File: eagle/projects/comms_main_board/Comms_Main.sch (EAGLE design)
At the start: 12 parts, among them U1 TPS562209DDCT, U2 LP2985-33DBVR

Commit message: Worked on comms power management portion of schematic more
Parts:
- added C10: 100nF, comms:CAP_100NF0_0805
- added C11: 22uF, comms:CAP_22UF0_1210
- added C12: 22uF, comms:CAP_22UF0_1206
- added C13: 4.7uF, comms:CAP_4UH7_0805
- added C8, C9: 1uF, comms:CAP_1UF0_0603
- added L2: 4.7uH, comms:L_4UH7
- added R3: 56.2k, comms:RES_56R2_0603
- added R4: 10k, comms:RES_10R0_0603
- added R5: 174k, comms:RES_174R0_0603
- added R6: 25.5k, comms:RES_25R5_0603
- added U3: LP5900TLX-3.3/NOPB, comms:LP5900TLX-3.3/NOPB
- added U4: TPS562209DDCT, comms:TPS562209DDCR
- added U5: LMZ34002RKGR, comms:LMZ34002RKGR
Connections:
- new net 11P1V_IN: C11.1, U4.EN, U4.VIN
- new net 12V_BOARD: R5.2
- new net 3P3V_ATV: C9.1, U3.VOUT
- new net 5V_BOARD: C12.1, C8.1, L2.2, R3.2, U3.VEN, U3.VIN
- new net N$5: C10.1, U4.VBST
- new net N$6: C10.2, L2.1, U4.SW
- new net N$7: R3.1, R4.2, U4.VFB
- new net N$8: C11.2, C12.2, R4.1, U4.GND
- new net N$9: R6.2
- net GND: now also C8.2, C9.2, U3.GND
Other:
- note added: "COMMS 11.1V Battery Power Management"

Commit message: Working on parts for comms power management more
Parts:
- added C14: 100uF, comms:CAP_100UF0_1206
- added R7: 53.6k, comms:RES_53R6_0603
- added U6: LM3488MMX/NOPB, comms:LM3488MMX/NOPB
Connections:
- new net N$10: R7.2
- new net NEG_5V_BOARD: U5.A_VOUT_2, U5.A_VOUT_3, U5.A_VOUT_5, U5.RT
- net GND: now also U5.GND_2, U5.GND_5
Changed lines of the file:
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@@
 <part name="R6" library="comms" deviceset="RES" device="_0603" technology="_25R5" value="25.5k"/>
 <part name="C13" library="comms" deviceset="CAP" device="_0805" technology="_4UH7" value="4.7uF"/>
+<part name="R7" library="comms" deviceset="RES" device="_0603" technology="_53R6" value="53.6k"/>
+<part name="SUPPLY4" library="supply2" deviceset="GND" device=""/>
+<part name="C14" library="comms" deviceset="CAP" device="_1206" technology="_100UF0" value="100uF"/>
+<part name="FRAME3" library="frames" deviceset="A4L-LOC" device=""/>
+<part name="U6" library="comms" deviceset="LM3488" device="" technology="MMX/NOPB" value="LM3488MMX/NOPB"/>
 </parts>
 <sheets>
@@
 <sheet>
 <plain>
+<text x="-67.056" y="73.66" size="5.08" layer="91">COMMS 11.1V Battery Power Management</text>
+</plain>
+<instances>
+<instance part="FRAME3" gate="G$1" x="-129.54" y="-93.98"/>
+<instance part="U6" gate="A" x="-33.02" y="2.54"/>
+</instances>
+<busses>
+</busses>
+<nets>
+</nets>
+</sheet>
+<sheet>
+<plain>
 <text x="108.966" y="115.316" size="5.08" layer="91">COMMS 11.1V Battery Power Management</text>
 </plain>
@@
 <instance part="R6" gate="G$1" x="68.58" y="27.94" rot="R90"/>
 <instance part="C13" gate="G$1" x="58.42" y="38.1"/>
+<instance part="R7" gate="G$1" x="149.86" y="-15.24" rot="R90"/>
+<instance part="SUPPLY4" gate="GND" x="119.38" y="-45.72"/>
+<instance part="C14" gate="G$1" x="170.18" y="27.94"/>
 </instances>
 <busses>
@@
 <pinref part="C8" gate="G$1" pin="2"/>
 <pinref part="C9" gate="G$1" pin="2"/>
+</segment>
+<segment>
+<wire x1="58.42" y1="35.814" x2="58.42" y2="-43.18" width="0.1524" layer="91"/>
+<wire x1="58.42" y1="-43.18" x2="119.38" y2="-43.18" width="0.1524" layer="91"/>
+<pinref part="SUPPLY4" gate="GND" pin="GND"/>
+<wire x1="119.38" y1="-43.18" x2="144.78" y2="-43.18" width="0.1524" layer="91"/>
+<junction x="119.38" y="-43.18"/>
+<wire x1="139.446" y1="-12.7" x2="144.78" y2="-12.7" width="0.1524" layer="91"/>
+<wire x1="144.78" y1="-12.7" x2="144.78" y2="-15.24" width="0.1524" layer="91"/>
+<junction x="144.78" y="-43.18"/>
+<pinref part="U5" gate="A" pin="GND_5"/>
+<wire x1="144.78" y1="-15.24" x2="144.78" y2="-17.78" width="0.1524" layer="91"/>
+<wire x1="144.78" y1="-17.78" x2="144.78" y2="-20.32" width="0.1524" layer="91"/>
+<wire x1="144.78" y1="-20.32" x2="144.78" y2="-22.86" width="0.1524" layer="91"/>
+<wire x1="144.78" y1="-22.86" x2="144.78" y2="-25.4" width="0.1524" layer="91"/>
+<wire x1="144.78" y1="-25.4" x2="144.78" y2="-27.94" width="0.1524" layer="91"/>
+<wire x1="144.78" y1="-27.94" x2="144.78" y2="-43.18" width="0.1524" layer="91"/>
+<wire x1="139.7" y1="-15.24" x2="144.78" y2="-15.24" width="0.1524" layer="91"/>
+<junction x="144.78" y="-15.24"/>
+<wire x1="139.446" y1="-17.78" x2="144.78" y2="-17.78" width="0.1524" layer="91"/>
+<junction x="144.78" y="-17.78"/>
+<wire x1="139.446" y1="-20.32" x2="144.78" y2="-20.32" width="0.1524" layer="91"/>
+<junction x="144.78" y="-20.32"/>
+<pinref part="U5" gate="A" pin="GND_2"/>
+<wire x1="139.7" y1="-22.86" x2="144.78" y2="-22.86" width="0.1524" layer="91"/>
+<junction x="144.78" y="-22.86"/>
+<wire x1="139.446" y1="-25.4" x2="144.78" y2="-25.4" width="0.1524" layer="91"/>
+<junction x="144.78" y="-25.4"/>
+<wire x1="139.446" y1="-27.94" x2="144.78" y2="-27.94" width="0.1524" layer="91"/>
+<junction x="144.78" y="-27.94"/>
+<wire x1="170.18" y1="25.654" x2="170.18" y2="-43.18" width="0.1524" layer="91"/>
+<wire x1="170.18" y1="-43.18" x2="149.86" y2="-43.18" width="0.1524" layer="91"/>
+<wire x1="149.86" y1="-43.18" x2="144.78" y2="-43.18" width="0.1524" layer="91"/>
+<wire x1="149.86" y1="-20.066" x2="149.86" y2="-43.18" width="0.1524" layer="91"/>
+<junction x="149.86" y="-43.18"/>
 </segment>
 </net>
@@
 <segment>
 <wire x1="101.854" y1="48.26" x2="68.58" y2="48.26" width="0.1524" layer="91"/>
-<label x="55.88" y="48.26" size="5.08" layer="95"/>
+<label x="55.88" y="48.26" size="1.778" layer="95"/>
 <pinref part="R5" gate="G$1" pin="2"/>
 <wire x1="68.58" y1="48.26" x2="58.42" y2="48.26" width="0.1524" layer="91"/>
@@
 </segment>
 </net>
+<net name="NEG_5V_BOARD" class="0">
+<segment>
+<wire x1="139.192" y1="48.26" x2="144.018" y2="48.26" width="0.1524" layer="91"/>
+<label x="172.72" y="48.26" size="1.778" layer="95"/>
+<wire x1="144.018" y1="48.26" x2="157.48" y2="48.26" width="0.1524" layer="91"/>
+<wire x1="157.48" y1="48.26" x2="170.18" y2="48.26" width="0.1524" layer="91"/>
+<wire x1="170.18" y1="48.26" x2="182.88" y2="48.26" width="0.1524" layer="91"/>
+<wire x1="139.446" y1="45.72" x2="144.018" y2="45.72" width="0.1524" layer="91"/>
+<wire x1="144.018" y1="45.72" x2="144.018" y2="48.26" width="0.1524" layer="91"/>
+<junction x="144.018" y="48.26"/>
+<wire x1="139.446" y1="43.18" x2="144.018" y2="43.18" width="0.1524" layer="91"/>
+<wire x1="144.018" y1="43.18" x2="144.018" y2="45.72" width="0.1524" layer="91"/>
+<junction x="144.018" y="45.72"/>
+<wire x1="139.192" y1="40.64" x2="144.018" y2="40.64" width="0.1524" layer="91"/>
+<wire x1="144.018" y1="40.64" x2="144.018" y2="43.18" width="0.1524" layer="91"/>
+<junction x="144.018" y="43.18"/>
+<wire x1="139.192" y1="38.1" x2="144.018" y2="38.1" width="0.1524" layer="91"/>
+<wire x1="144.018" y1="38.1" x2="144.018" y2="40.64" width="0.1524" layer="91"/>
+<junction x="144.018" y="40.64"/>
+<wire x1="139.446" y1="35.56" x2="144.018" y2="35.56" width="0.1524" layer="91"/>
+<wire x1="144.018" y1="35.56" x2="144.018" y2="38.1" width="0.1524" layer="91"/>
+<junction x="144.018" y="38.1"/>
+<wire x1="170.18" y1="32.766" x2="170.18" y2="48.26" width="0.1524" layer="91"/>
+<junction x="170.18" y="48.26"/>
+<pinref part="U5" gate="A" pin="RT"/>
+<wire x1="139.7" y1="30.48" x2="157.48" y2="30.48" width="0.1524" layer="91"/>
+<wire x1="157.48" y1="30.48" x2="157.48" y2="48.26" width="0.1524" layer="91"/>
+<junction x="157.48" y="48.26"/>
+<wire x1="157.48" y1="30.48" x2="157.48" y2="22.86" width="0.1524" layer="91"/>
+<junction x="157.48" y="30.48"/>
+<wire x1="157.48" y1="22.86" x2="157.48" y2="20.32" width="0.1524" layer="91"/>
+<wire x1="157.48" y1="20.32" x2="157.48" y2="11.684" width="0.1524" layer="91"/>
+<wire x1="139.446" y1="12.7" x2="147.32" y2="12.7" width="0.1524" layer="91"/>
+<pinref part="U5" gate="A" pin="A_VOUT_3"/>
+<wire x1="147.32" y1="12.7" x2="147.32" y2="11.684" width="0.1524" layer="91"/>
+<wire x1="147.32" y1="11.684" x2="147.32" y2="10.16" width="0.1524" layer="91"/>
+<wire x1="147.32" y1="10.16" x2="147.32" y2="7.62" width="0.1524" layer="91"/>
+<wire x1="147.32" y1="7.62" x2="147.32" y2="5.08" width="0.1524" layer="91"/>
+<wire x1="147.32" y1="5.08" x2="147.32" y2="2.54" width="0.1524" layer="91"/>
+<wire x1="147.32" y1="2.54" x2="147.32" y2="0" width="0.1524" layer="91"/>
+<wire x1="147.32" y1="0" x2="147.32" y2="-2.54" width="0.1524" layer="91"/>
+<wire x1="147.32" y1="-2.54" x2="139.7" y2="-2.54" width="0.1524" layer="91"/>
+<wire x1="139.446" y1="0" x2="147.32" y2="0" width="0.1524" layer="91"/>
+<junction x="147.32" y="0"/>
+<pinref part="U5" gate="A" pin="A_VOUT_5"/>
+<wire x1="139.7" y1="2.54" x2="147.32" y2="2.54" width="0.1524" layer="91"/>
+<junction x="147.32" y="2.54"/>
+<pinref part="U5" gate="A" pin="A_VOUT_2"/>
+<wire x1="139.7" y1="5.08" x2="147.32" y2="5.08" width="0.1524" layer="91"/>
+<junction x="147.32" y="5.08"/>
+<wire x1="139.446" y1="7.62" x2="147.32" y2="7.62" width="0.1524" layer="91"/>
+<junction x="147.32" y="7.62"/>
+<wire x1="139.446" y1="10.16" x2="147.32" y2="10.16" width="0.1524" layer="91"/>
+<junction x="147.32" y="10.16"/>
+<wire x1="147.32" y1="11.684" x2="157.48" y2="11.684" width="0.1524" layer="91"/>
+<junction x="147.32" y="11.684"/>
+<wire x1="157.48" y1="11.684" x2="157.48" y2="-38.1" width="0.1524" layer="91"/>
+<junction x="157.48" y="11.684"/>
+<wire x1="157.48" y1="-38.1" x2="76.2" y2="-38.1" width="0.1524" layer="91"/>
+<wire x1="76.2" y1="-38.1" x2="68.58" y2="-38.1" width="0.1524" layer="91"/>
+<wire x1="68.58" y1="-38.1" x2="68.58" y2="23.622" width="0.1524" layer="91"/>
+<wire x1="102.616" y1="33.02" x2="76.2" y2="33.02" width="0.1524" layer="91"/>
+<wire x1="76.2" y1="33.02" x2="76.2" y2="-38.1" width="0.1524" layer="91"/>
+<junction x="76.2" y="-38.1"/>
+<wire x1="139.446" y1="22.86" x2="157.48" y2="22.86" width="0.1524" layer="91"/>
+<junction x="157.48" y="22.86"/>
+<wire x1="139.446" y1="20.32" x2="157.48" y2="20.32" width="0.1524" layer="91"/>
+<junction x="157.48" y="20.32"/>
+</segment>
+</net>
+<net name="N$10" class="0">
+<segment>
+<wire x1="139.446" y1="-7.62" x2="149.86" y2="-7.62" width="0.1524" layer="91"/>
+<pinref part="R7" gate="G$1" pin="2"/>
+<wire x1="149.86" y1="-10.16" x2="149.86" y2="-7.62" width="0.1524" layer="91"/>
+</segment>
+</net>

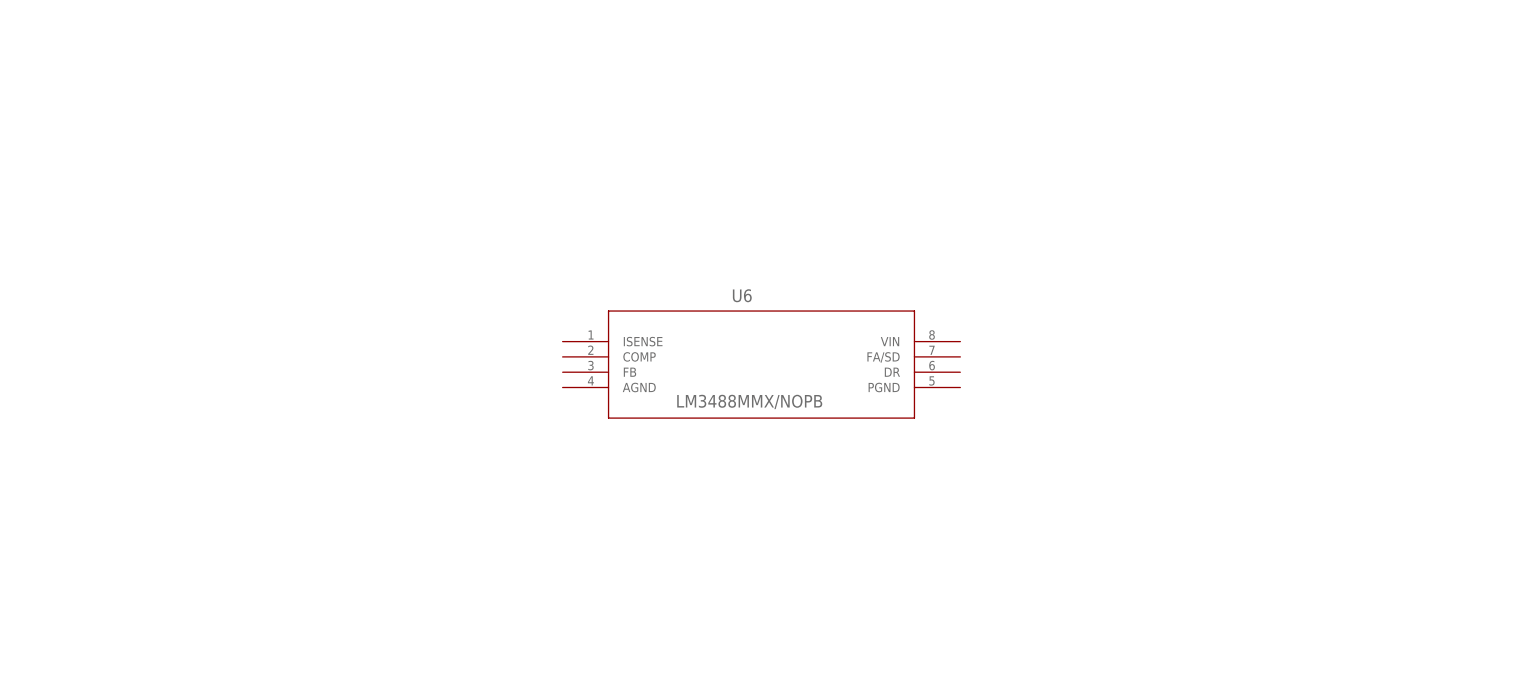
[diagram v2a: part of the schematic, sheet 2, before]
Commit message: Finished comms power management schematic
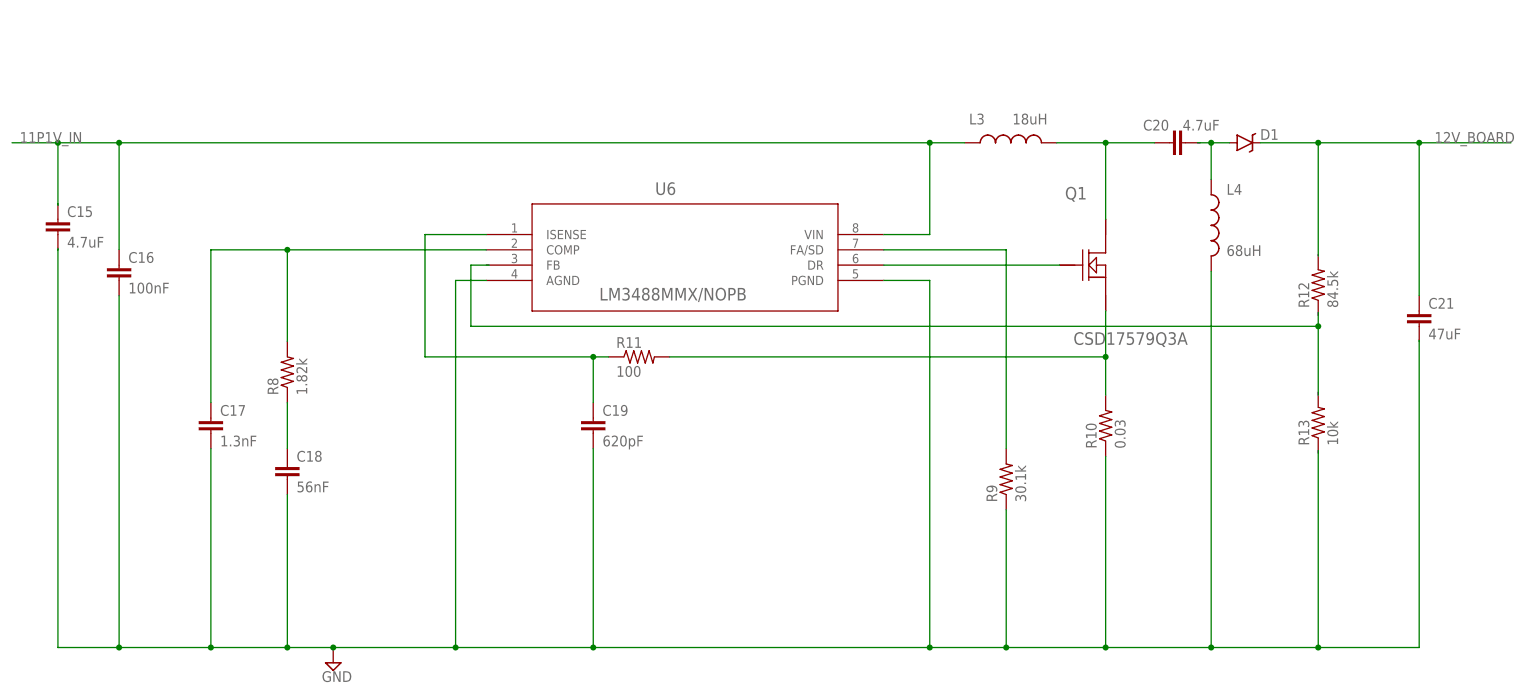
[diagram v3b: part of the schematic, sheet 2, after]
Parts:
- added C15: 4.7uF, comms:CAP_4UH7_1210
- added C16: 100nF, comms:CAP_100NF0_0805
- added C17: 1.3nF, comms:CAP_1NF3_0805
- added C18: 56nF, comms:CAP_56NF0_0603
- added C19: 620pF, comms:CAP_620PF0_0805
- added C20: 4.7uF, comms:CAP_4UH7_0805
- added C21: 47uF, comms:CAP_47UF0_1210
- added D1: (no value), comms:DIODE-SCHOTTKY_DO-214AC
- added L3: 18uH, comms:L_18UH0-180ML
- added L4: 68uH, comms:L_68UH0-680ML
- added Q1: CSD17579Q3A, comms:CSD17579Q3A
- added R10: 0.03, comms:RES_0RS030_0805
- added R11: 100, comms:RES_0R100_0603
- added R12: 84.5k, comms:RES_84R5_0603
- added R13: 10k, comms:RES_10R0_0603
- added R8: 1.82k, comms:RES_1R82_0805
- added R9: 30.1k, comms:RES_30R1_0603
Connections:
- new net N$11: U5.PH, U5.PH_2, U5.PH_3, U5.PH_4, U5.PH_5
- new net N$12: C18.1, R8.1
- new net N$13: C17.1, R8.2, U6.COMP
- new net N$14: R9.2, U6.FA/SD
- new net N$15: C19.1, R11.1, U6.ISENSE
- new net N$16: Q1.GATE, U6.DR
- new net N$17: Q1.SOURCE_2, R10.2, R11.2
- new net N$18: C20.1, L3.2, Q1.DRAIN_2
- new net N$19: D1.A, L4.1
- net 11P1V_IN: now also C15.1, C16.1, L3.1, U6.VIN
- net 12V_BOARD: now also C21.1, D1.C
- net GND: now also C15.2, C16.2, C17.2, C18.2, C19.2, L4.2, R10.1, R9.1, U6.AGND, U6.PGND
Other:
- moved on the sheet: U6

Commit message: Max-m8q gps sch
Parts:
- added C22: 10nF, comms:CAP_10NF0_0805
- added J1: RECE-20279-001E, comms:IPEX-20279-001E
- added L5: 27nH, comms:L_27NH0_0603
- added R14, R15: 4.7k, daqcs:RES_4R7_0603
- added R16: 10, comms:RES_0R10_0603
- added U$1: MAX-M8Q, comms:UBLOX_MAX
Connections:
- new net 3P3V_ACC: R14.2, R15.2
- new net GPS_SCL: R15.1, U$1.17_SCL2
- new net GPS_SDA: R14.1, U$1.16_SDA2
- new net N$20: R16.2, U$1.15_RESERVED
- new net N$22: C22.1, R16.1
- new net N$24: J1.1, L5.1, U$1.11_RF_IN
- net 3P3V_SENSORS: now also U$1.6_V_BCKP, U$1.7_VCC_IO, U$1.8_VCC
- net GND: now also C22.2, J1.GND@1, U$1.10_GND, U$1.12_GND, U$1.1_GND
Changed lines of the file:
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@@
 <part name="C21" library="comms" deviceset="CAP" device="_1210" technology="_47UF0" value="47uF"/>
 <part name="L4" library="comms" deviceset="L" device="-680ML" technology="_68UH0" value="68uH"/>
+<part name="FRAME4" library="frames" deviceset="A4L-LOC" device=""/>
+<part name="U$1" library="comms" deviceset="UBLOX_MAX" device="" value="MAX-M8Q"/>
+<part name="R14" library="daqcs" deviceset="RES" device="_0603" technology="_4R7" value="4.7k"/>
+<part name="R15" library="daqcs" deviceset="RES" device="_0603" technology="_4R7" value="4.7k"/>
+<part name="SUPPLY6" library="supply2" deviceset="GND" device=""/>
+<part name="J1" library="comms" deviceset="IPEX-20279-001E" device="" value="RECE-20279-001E"/>
+<part name="R16" library="comms" deviceset="RES" device="_0603" technology="_0R10" value="10"/>
+<part name="C22" library="comms" deviceset="CAP" device="_0805" technology="_10NF0" value="10nF"/>
+<part name="L5" library="comms" deviceset="L" device="_0603" technology="_27NH0" value="27nH"/>
 </parts>
 <sheets>
@@
 </segment>
 </net>
+</nets>
+</sheet>
+<sheet>
+<plain>
+</plain>
+<instances>
+<instance part="FRAME4" gate="G$1" x="0" y="0"/>
+<instance part="U$1" gate="G$1" x="134.62" y="106.68"/>
+<instance part="R14" gate="G$1" x="50.8" y="101.6" rot="R90"/>
+<instance part="R15" gate="G$1" x="38.1" y="101.6" rot="R90"/>
+<instance part="SUPPLY6" gate="GND" x="99.06" y="68.58"/>
+<instance part="J1" gate="G$1" x="55.88" y="116.84"/>
+<instance part="R16" gate="G$1" x="91.44" y="96.52"/>
+<instance part="C22" gate="G$1" x="76.2" y="78.74"/>
+<instance part="L5" gate="G$1" x="76.2" y="104.14"/>
+</instances>
+<busses>
+</busses>
+<nets>
+<net name="3P3V_SENSORS" class="0">
+<segment>
+<pinref part="U$1" gate="G$1" pin="8_VCC"/>
+<wire x1="157.48" y1="116.84" x2="170.18" y2="116.84" width="0.1524" layer="91"/>
+<pinref part="U$1" gate="G$1" pin="7_VCC_IO"/>
+<wire x1="170.18" y1="116.84" x2="195.58" y2="116.84" width="0.1524" layer="91"/>
+<wire x1="157.48" y1="111.76" x2="170.18" y2="111.76" width="0.1524" layer="91"/>
+<pinref part="U$1" gate="G$1" pin="6_V_BCKP"/>
+<wire x1="157.48" y1="106.68" x2="170.18" y2="106.68" width="0.1524" layer="91"/>
+<wire x1="170.18" y1="106.68" x2="170.18" y2="111.76" width="0.1524" layer="91"/>
+<label x="175.26" y="116.84" size="1.778" layer="95"/>
+<wire x1="170.18" y1="116.84" x2="170.18" y2="111.76" width="0.1524" layer="91"/>
+<junction x="170.18" y="116.84"/>
+<junction x="170.18" y="111.76"/>
+</segment>
+</net>
+<net name="3P3V_ACC" class="0">
+<segment>
+<pinref part="R15" gate="G$1" pin="2"/>
+<wire x1="38.1" y1="106.68" x2="38.1" y2="109.22" width="0.1524" layer="91"/>
+<wire x1="38.1" y1="109.22" x2="10.16" y2="109.22" width="0.1524" layer="91"/>
+<pinref part="R14" gate="G$1" pin="2"/>
+<wire x1="50.8" y1="106.68" x2="50.8" y2="109.22" width="0.1524" layer="91"/>
+<wire x1="50.8" y1="109.22" x2="38.1" y2="109.22" width="0.1524" layer="91"/>
+<label x="12.7" y="109.22" size="1.778" layer="95"/>
+</segment>
+</net>
+<net name="GND" class="0">
+<segment>
+<pinref part="SUPPLY6" gate="GND" pin="GND"/>
+<wire x1="99.06" y1="121.92" x2="99.06" y2="114.3" width="0.1524" layer="91"/>
+<wire x1="99.06" y1="114.3" x2="99.06" y2="111.76" width="0.1524" layer="91"/>
+<wire x1="99.06" y1="111.76" x2="99.06" y2="76.2" width="0.1524" layer="91"/>
+<wire x1="99.06" y1="76.2" x2="99.06" y2="73.66" width="0.1524" layer="91"/>
+<wire x1="99.06" y1="73.66" x2="99.06" y2="71.12" width="0.1524" layer="91"/>
+<pinref part="U$1" gate="G$1" pin="12_GND"/>
+<wire x1="111.76" y1="111.76" x2="99.06" y2="111.76" width="0.1524" layer="91"/>
+<junction x="99.06" y="111.76"/>
+<wire x1="170.18" y1="81.28" x2="170.18" y2="73.66" width="0.1524" layer="91"/>
+<pinref part="U$1" gate="G$1" pin="1_GND"/>
+<wire x1="157.48" y1="81.28" x2="170.18" y2="81.28" width="0.1524" layer="91"/>
+<wire x1="170.18" y1="73.66" x2="99.06" y2="73.66" width="0.1524" layer="91"/>
+<junction x="99.06" y="73.66"/>
+<pinref part="U$1" gate="G$1" pin="10_GND"/>
+<wire x1="111.76" y1="121.92" x2="99.06" y2="121.92" width="0.1524" layer="91"/>
+<pinref part="J1" gate="G$1" pin="GND@1"/>
+<wire x1="58.42" y1="114.3" x2="99.06" y2="114.3" width="0.1524" layer="91"/>
+<junction x="99.06" y="114.3"/>
+<pinref part="C22" gate="G$1" pin="2"/>
+<wire x1="76.2" y1="76.2" x2="99.06" y2="76.2" width="0.1524" layer="91"/>
+<junction x="99.06" y="76.2"/>
+</segment>
+</net>
+<net name="N$24" class="0">
+<segment>
+<pinref part="J1" gate="G$1" pin="1"/>
+<pinref part="U$1" gate="G$1" pin="11_RF_IN"/>
+<wire x1="58.42" y1="116.84" x2="76.2" y2="116.84" width="0.1524" layer="91"/>
+<pinref part="L5" gate="G$1" pin="1"/>
+<wire x1="76.2" y1="116.84" x2="111.76" y2="116.84" width="0.1524" layer="91"/>
+<wire x1="76.2" y1="111.76" x2="76.2" y2="116.84" width="0.1524" layer="91"/>
+<junction x="76.2" y="116.84"/>
+</segment>
+</net>
+<net name="GPS_SCL" class="0">
+<segment>
+<pinref part="R15" gate="G$1" pin="1"/>
+<wire x1="38.1" y1="96.52" x2="38.1" y2="86.36" width="0.1524" layer="91"/>
+<pinref part="U$1" gate="G$1" pin="17_SCL2"/>
+<wire x1="38.1" y1="86.36" x2="111.76" y2="86.36" width="0.1524" layer="91"/>
+<wire x1="38.1" y1="86.36" x2="10.16" y2="86.36" width="0.1524" layer="91"/>
+<junction x="38.1" y="86.36"/>
+<label x="12.7" y="86.36" size="1.778" layer="95"/>
+</segment>
+</net>
+<net name="GPS_SDA" class="0">
+<segment>
+<pinref part="U$1" gate="G$1" pin="16_SDA2"/>
+<wire x1="111.76" y1="91.44" x2="50.8" y2="91.44" width="0.1524" layer="91"/>
+<pinref part="R14" gate="G$1" pin="1"/>
+<wire x1="50.8" y1="91.44" x2="50.8" y2="96.52" width="0.1524" layer="91"/>
+<wire x1="50.8" y1="91.44" x2="10.16" y2="91.44" width="0.1524" layer="91"/>
+<junction x="50.8" y="91.44"/>
+<label x="12.7" y="91.44" size="1.778" layer="95"/>
+</segment>
+</net>
+<net name="N$22" class="0">
+<segment>
+<pinref part="R16" gate="G$1" pin="1"/>
+<wire x1="86.36" y1="96.52" x2="76.2" y2="96.52" width="0.1524" layer="91"/>
+<pinref part="C22" gate="G$1" pin="1"/>
+<wire x1="76.2" y1="96.52" x2="76.2" y2="83.82" width="0.1524" layer="91"/>
+</segment>
+</net>
+<net name="N$20" class="0">
+<segment>
+<pinref part="R16" gate="G$1" pin="2"/>
+<pinref part="U$1" gate="G$1" pin="15_RESERVED"/>
+<wire x1="96.52" y1="96.52" x2="111.76" y2="96.52" width="0.1524" layer="91"/>
+</segment>
+</net>
